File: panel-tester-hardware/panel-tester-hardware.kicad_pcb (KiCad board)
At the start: 2 copper layers, 51.5 x 53.5 mm, 21 parts, among them J1 Screw_Terminal_01x02, J2 Conn_01x02, J3 Conn_01x07, Q2 BS170, U3 LM358, U4 INA219AxD

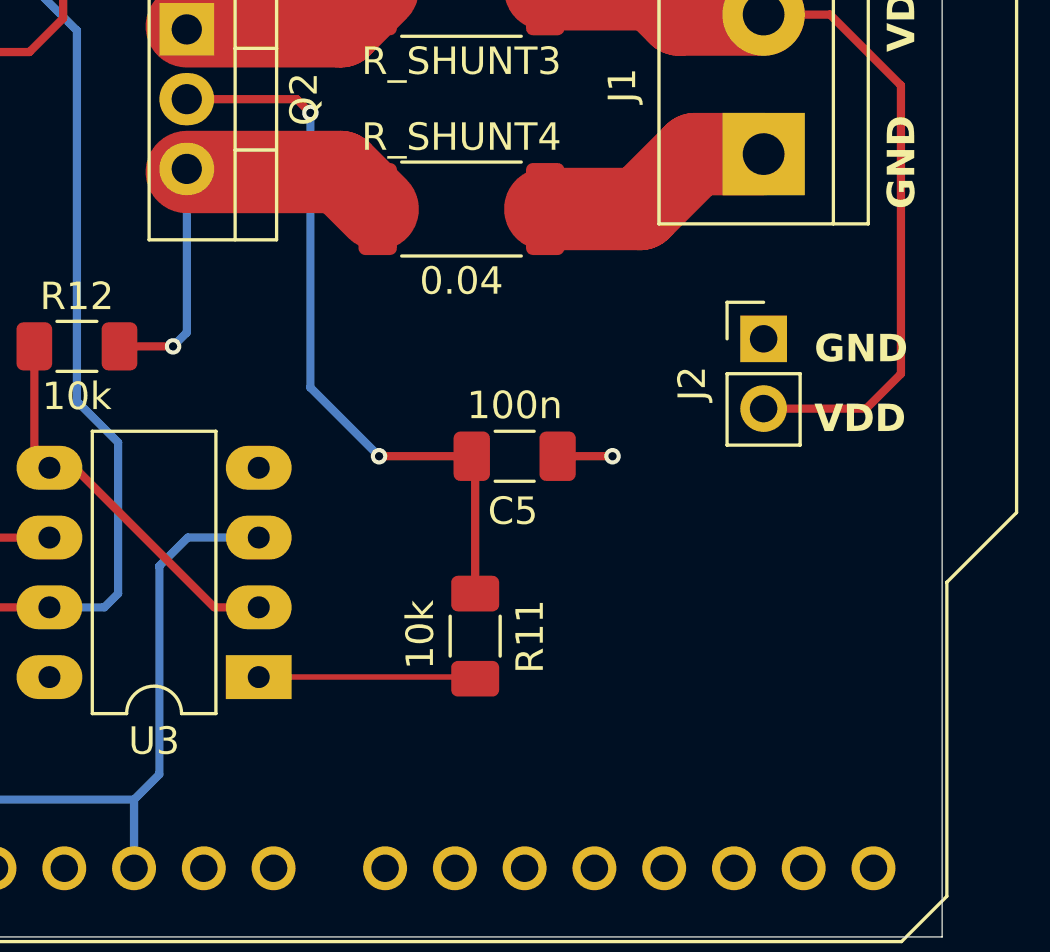
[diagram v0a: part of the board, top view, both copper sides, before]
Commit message: Made final slikscreen changes
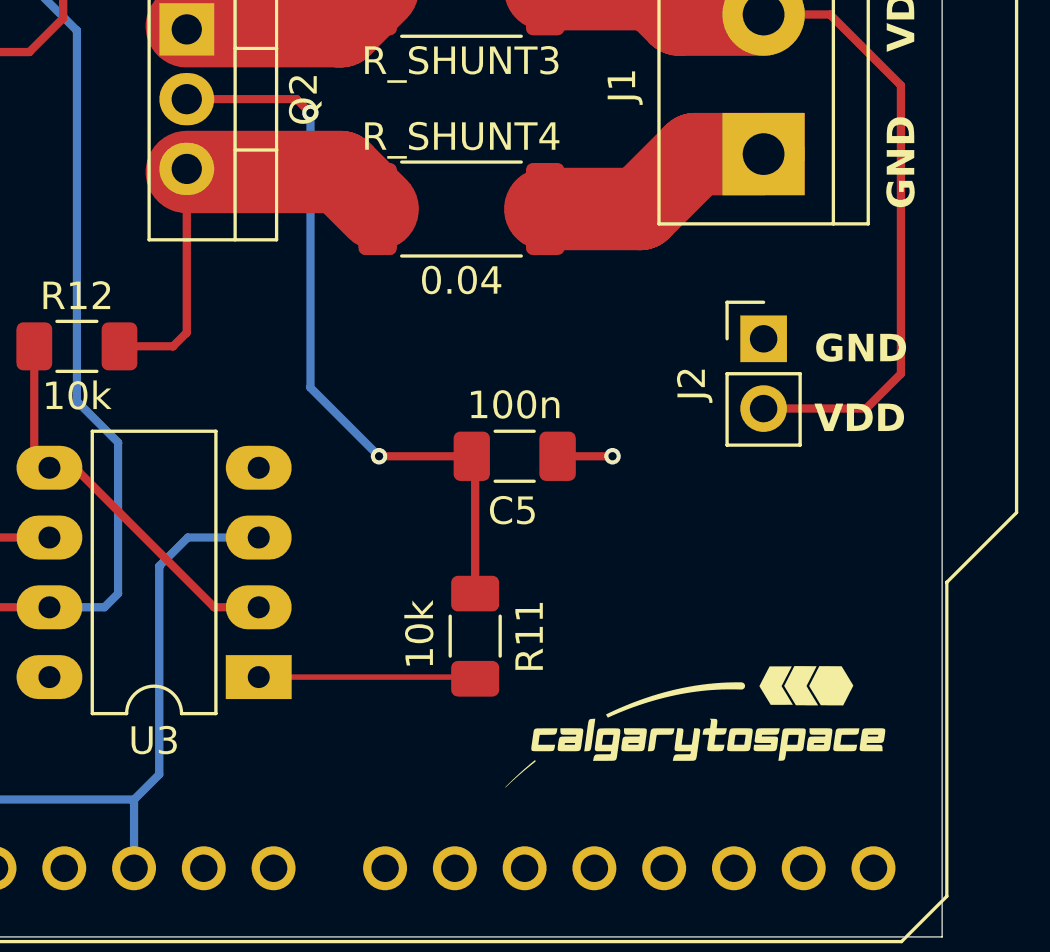
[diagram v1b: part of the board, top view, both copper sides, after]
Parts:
- added G***: LOGO, LOGO, F.Cu at (152.4, 82.2)
- added G***: LOGO, LOGO, B.Cu at (118.2, 43.2)
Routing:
- net Net-(Q2-S): vias 1 -> 0
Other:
- board text added: "2024-05-07 Rev. 1"

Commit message: Completed routing and aesthetic fixes
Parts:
- removed the G*** at (152.4, 82.2)
- added C1: 0.1u, Capacitor_SMD:C_1206_3216Metric_Pad1.33x1.80mm_HandSolder, F.Cu at (129.2, 79.0)
- added R5: 10k, Resistor_SMD:R_1206_3216Metric_Pad1.30x1.75mm_HandSolder, F.Cu at (144.5, 79.8)
- added R6: 10k, Resistor_SMD:R_1206_3216Metric_Pad1.30x1.75mm_HandSolder, F.Cu at (150.1, 81.2)
- added U1: MCP4921, Package_SO:SOIC-8_3.9x4.9mm_P1.27mm, F.Cu at (135.9, 81.4)
- moved C5 7.27 mm to (139.8, 68.6), turned to 0 degrees
- moved R12 6.48 mm to (127.8, 62.4)
- moved R11 5.83 mm to (139.8, 75.6), turned to 0 degrees
- moved R9 5.68 mm to (122.0, 63.8)
- moved U3 5.67 mm to (134.2, 75.4)
- moved R10 5.57 mm to (122.0, 70.4)
- moved C8 5.35 mm to (121.4, 75.8)
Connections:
- A1 pad 18: unconnected-(A1-D3-Pad18) -> DAC_MOSI
- A1 pad 25: MCU_MOSFET_CTRL -> DAC_CS
- A1 pad 28: unconnected-(A1-D13-Pad28) -> DAC_SCK
- J3 pad 6: MCU_MOSFET_CTRL -> DAC_OUTPUT
- U3 pad 3: MCU_MOSFET_CTRL -> Net-(U3A-+)
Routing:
- net MCU_MOSFET_CTRL: track 49.3 -> 0.00 mm
- net DAC_OUTPUT: track 0.00 -> 38.9 mm, vias 0 -> 1
- net Net-(U3A-+): track 0.00 -> 23.6 mm, vias 0 -> 1
- net DAC_MOSI: track 0.00 -> 20.5 mm
- net DAC_SCK: track 0.00 -> 13.0 mm
- net GND: track 29.6 -> 39.6 mm, vias 6 -> 10
- net DAC_CS: track 0.00 -> 9.51 mm, vias 0 -> 1
- net MCU_ALT_CURRENT_SENSE: track 67.6 -> 61.1 mm
- net Net-(Q2-S): track 16.1 -> 12.3 mm
- net Net-(R11-Pad1): track 7.40 -> 4.11 mm
- net Net-(U3B--): track 11.4 -> 8.71 mm
- net Net-(U3A--): track 14.4 -> 16.8 mm
- net +3V3: track 1.22 -> 0.69 mm
- net Net-(Q2-G): vias 2 -> 1
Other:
- board text added: "2024-05-18 Rev. 1.1"
- board text added: "DACO"
- board text removed: "2024-05-07 Rev. 1"
- board text removed: "FET"

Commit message: Created production files
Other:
- board text added: "2024-05-18 Rev. 2"
- board text removed: "2024-05-18 Rev. 1.1"
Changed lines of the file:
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@@
 		(tags "resistor handsolder")
 		(property "Reference" "R11"
-			(at 0 -2 360)
+			(at 0 -2 0)
 			(layer "F.SilkS")
 			(effects
@@
 		)
 		(property "Value" "10k"
-			(at 4 0 360)
+			(at 4 0 0)
 			(layer "F.SilkS")
 			(effects
@@
 		)
 		(fp_text user "${REFERENCE}"
-			(at 0 0 360)
+			(at 0 0 0)
 			(layer "F.Fab")
 			(effects
@@
 		(tags "capacitor handsolder")
 		(property "Reference" "C5"
-			(at 0.0625 -2 360)
+			(at 0.0625 -2 0)
 			(layer "F.SilkS")
 			(effects
@@
 		)
 		(fp_text user "${REFERENCE}"
-			(at 0 0 360)
+			(at 0 0 0)
 			(layer "F.Fab")
 			(effects
@@
 		(tags "capacitor handsolder")
 		(property "Reference" "C1"
-			(at 0 2 360)
+			(at 0 2 0)
 			(layer "F.SilkS")
 			(effects
@@
 		)
 		(fp_text user "${REFERENCE}"
-			(at 0 0 360)
+			(at 0 0 0)
 			(layer "F.Fab")
 			(effects
@@
 		)
 		(property "Value" "MCP4921"
-			(at 0 3.4 360)
+			(at 0 3.4 0)
 			(layer "F.Fab")
 			(effects
@@
 		)
 		(fp_text user "${REFERENCE}"
-			(at 0 0 360)
+			(at 0 0 0)
 			(layer "F.Fab")
 			(effects
@@
 		(layer "Edge.Cuts")
 	)
-	(gr_text "2024-05-18\nRev. 1.1\n"
+	(gr_text "2024-05-18\nRev. 2\n"
 		(at 160 44.8 0)
 		(layer "B.SilkS")
